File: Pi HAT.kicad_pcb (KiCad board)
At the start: 4 copper layers, 65 x 41.5 mm, 72 parts, among them IC1 AD7730, J1 Screw_Terminal_01x04, J11 Conn_01x02_Male, J4 Barrel_Jack, J5 Screw_Terminal_01x03, J6 Screw_Terminal_01x03, J7 GPIO_CONNECTOR, J9 Conn_01x03_Male, K1 SANYOU_SRD_Form_C, K2 SANYOU_SRD_Form_C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

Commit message: Updated wiring. Test points only added for AD7730.
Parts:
- removed TP1, TP2, TP3, TP4: TestPoint, TestPoint:TestPoint_Pad_D1.5mm
- moved R5 8.51 mm to (127.5, 106.7)
- moved R3 0.20 mm to (148.2, 123.0)
- moved C1 0.15 mm to (174.3, 108.6)
- moved C2 0.15 mm to (174.3, 105.6)
- moved R15 0.11 mm to (129.7, 117.6)
- moved C9 0.10 mm to (129.8, 118.6)
- moved JP2 0.08 mm to (137.1, 108.8)
- moved C12 0.06 mm to (125.2, 128.1)
- moved JP3 0.06 mm to (151.3, 108.8)
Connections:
- U1 pad 1: /GPIO16_SPI_CE2_N -> /GPIO8_SPI_CE0_N
- U1 pad 10: /GPIO16_SPI_CE2_N -> /GPIO8_SPI_CE0_N
- U1 pad 11: /GPIO19_SPI_MISO -> /GPIO9_SPI_MISO
- U1 pad 13: /GPIO16_SPI_CE2_N -> /GPIO8_SPI_CE0_N
- U1 pad 2: /GPIO21_SPI_SCLK -> /GPIO11_SPI_SCLK
- U1 pad 4: /GPIO16_SPI_CE2_N -> /GPIO8_SPI_CE0_N
- U1 pad 5: /GPIO20_SPI_MOSI -> /GPIO10_SPI_MOSI
- U1 pad 9: /GPIO16_SPI_CE2_N -> /GPIO8_SPI_CE0_N
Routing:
- net /GPIO8_SPI_CE0_N: track 0.00 -> 93.6 mm, vias 0 -> 5
- net +3V3: track 9.73 -> 82.4 mm, vias 0 -> 5
- net /GPIO9_SPI_MISO: track 31.5 -> 81.8 mm, vias 1 -> 3
- net /GPIO11_SPI_SCLK: track 34.3 -> 77.9 mm, vias 1 -> 2
- net /GPIO10_SPI_MOSI: track 30.3 -> 71.6 mm, vias 1 -> 3
- net /GPIO22_GEN3: track 0.00 -> 29.3 mm
- net GND: track 11.0 -> 36.3 mm, vias 0 -> 11
- net /GPIO16_SPI_CE2_N: track 22.1 -> 0.00 mm, vias 3 -> 0
- net /GPIO26: track 28.2 -> 11.4 mm
- net +5V: track 55.9 -> 70.6 mm
- net /GPIO20_SPI_MOSI: track 13.2 -> 0.00 mm
- net /Power Monitor/ADC0: track 0.00 -> 13.2 mm, vias 0 -> 1
- net Net-(JP6-Pad1): track 0.00 -> 11.9 mm, vias 0 -> 2
- net /Relays/COM2: track 17.7 -> 29.2 mm, vias 0 -> 3
- net /GPIO21_SPI_SCLK: track 11.1 -> 0.00 mm, vias 1 -> 0
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- removed copper zone on F.Cu, net GND
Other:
- copper layers 4 -> 2
- board text added: "Jumper"

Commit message: Updated wiring.
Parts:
- added G***: LOGO, LOGO, F.Cu at (172.4, 124.0)
- moved R9 2.69 mm to (119.4, 112.5), turned to 180 degrees
- moved D3 1.99 mm to (119.8, 110.3), turned to 90 degrees
- moved R16 0.19 mm to (158.1, 121.9)
- moved D1 0.19 mm to (156.5, 120.2)
- moved D4 0.19 mm to (155.6, 122.2)
- moved D5 0.17 mm to (138.7, 122.3)
- moved J9 0.14 mm to (125.0, 130.5)
- moved D2 0.09 mm to (139.5, 120.3)
- moved R17 0.09 mm to (141.2, 122.0)
- moved C1 0.06 mm to (174.3, 108.6)
- moved C2 0.06 mm to (174.3, 105.6)
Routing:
- net +5V: track 70.6 -> 197.1 mm, vias 2 -> 14
- net /GPIO5: track 0.00 -> 54.4 mm, vias 0 -> 2
- net GND: track 36.3 -> 75.7 mm, vias 11 -> 15
- net /GPIO26: track 11.4 -> 33.4 mm, vias 2 -> 4
- net /Relays/DC_SIDE2: track 16.4 -> 25.5 mm
- net /GPIO8_SPI_CE0_N: track 93.6 -> 96.5 mm
- net /Power Monitor/ADC0: track 13.2 -> 11.2 mm
- net /GPIO10_SPI_MOSI: track 71.6 -> 72.6 mm
- net /GPIO11_SPI_SCLK: track 77.9 -> 78.8 mm
- net /GPIO9_SPI_MISO: track 81.8 -> 82.7 mm
- net /Power Monitor/ADC6: track 15.4 -> 14.6 mm
- net /Power Monitor/ADC7: track 12.6 -> 13.3 mm
- net /Relays/DC_SIDE1: track 24.6 -> 24.9 mm, vias 0 -> 1
- added copper zone on F.Cu, net +5V
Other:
- board text added: "Pi Zero HAT Montso Mokake XX/12/2022"

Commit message: Updated via sizes on wiring.
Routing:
- net GND: track 75.7 -> 77.3 mm, vias 15 -> 17
- net +3V3: track 82.4 -> 83.2 mm, vias 5 -> 6
- net +5V: track 197.1 -> 197.7 mm, vias 14 -> 16

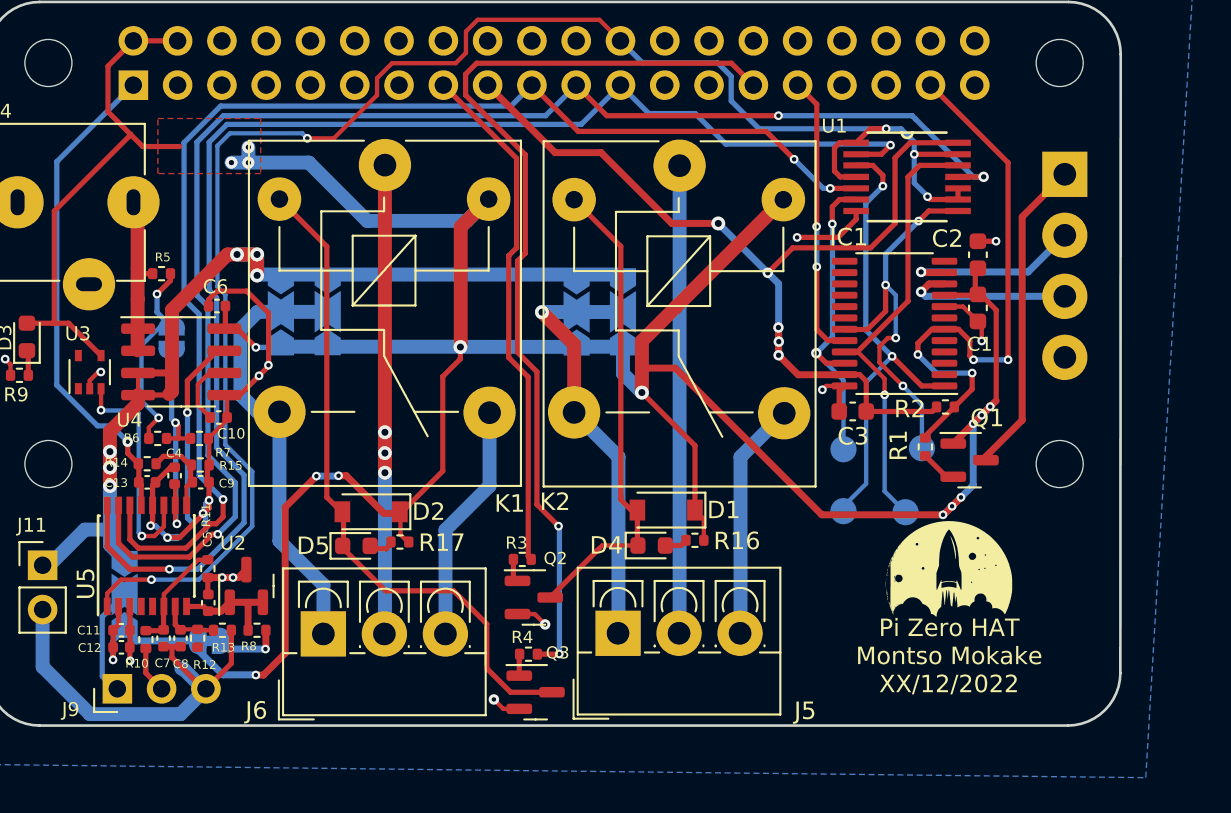
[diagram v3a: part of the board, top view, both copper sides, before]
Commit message: Used Phoenix connectors. Wired ADC0 track.
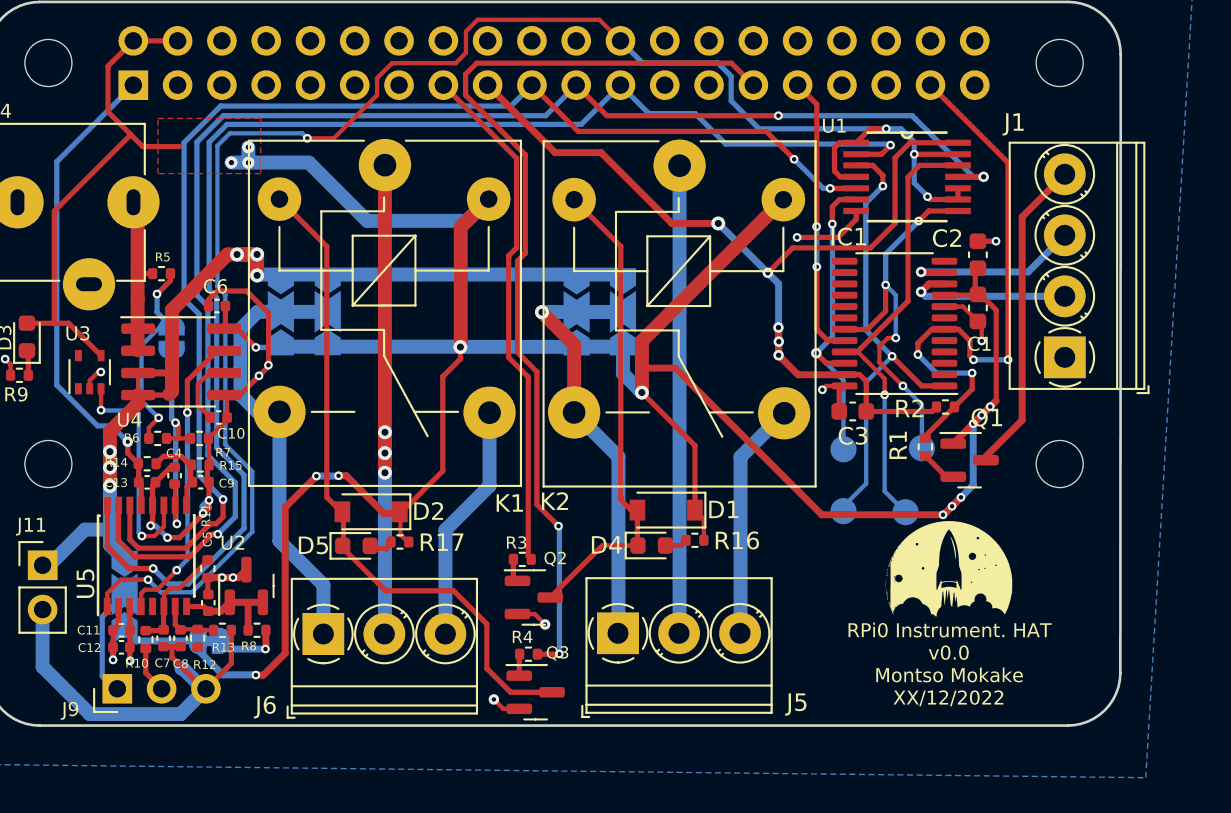
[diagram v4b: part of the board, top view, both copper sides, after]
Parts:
- J1: footprint TerminalBlock_4Ucon:TerminalBlock_4Ucon_1x04_P3.50mm_Vertical -> TerminalBlock_Phoenix:TerminalBlock_Phoenix_PT-1,5-4-3.5-H_1x04_P3.50mm_Horizontal; moved to F.Cu
- J5, J6: footprint TerminalBlock_4Ucon:TerminalBlock_4Ucon_1x03_P3.50mm_Vertical -> TerminalBlock_Phoenix:TerminalBlock_Phoenix_PT-1,5-3-3.5-H_1x03_P3.50mm_Horizontal
- moved J1 10.5 mm to (179.3, 111.5), turned to 90 degrees
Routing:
- net /Power Monitor/ADC0: track 11.2 -> 17.3 mm, vias 1 -> 2
- net GND: track 77.3 -> 75.8 mm
- net /GPIO11_SPI_SCLK: track 78.6 -> 79.4 mm
- net /GPIO8_SPI_CE0_N: track 96.1 -> 96.9 mm
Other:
- board text added: "RPi0 Instrument. HAT v0.0 Montso Mokake XX/12/2022"
- board text removed: "Pi Zero HAT Montso Mokake XX/12/2022"

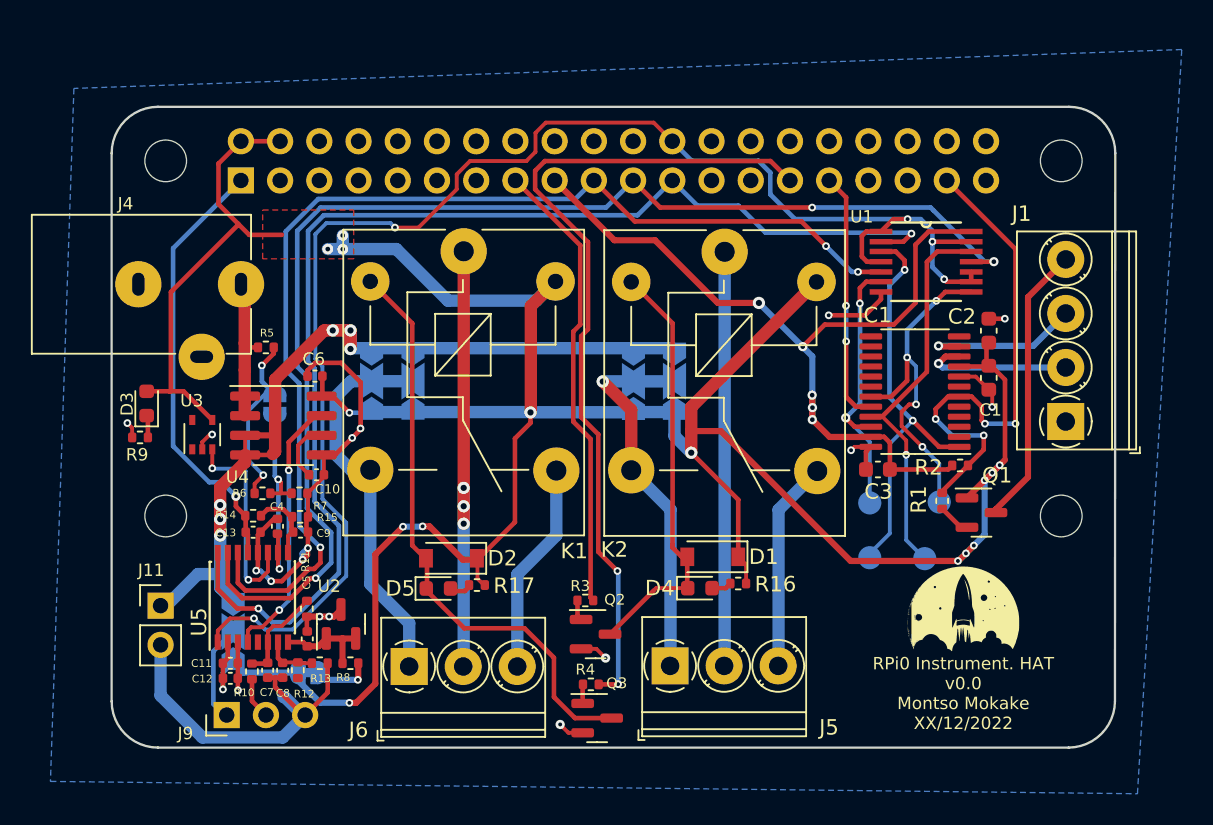
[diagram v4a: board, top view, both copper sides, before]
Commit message: Fixed CE pins. Added GND copper pour on F.Cu.
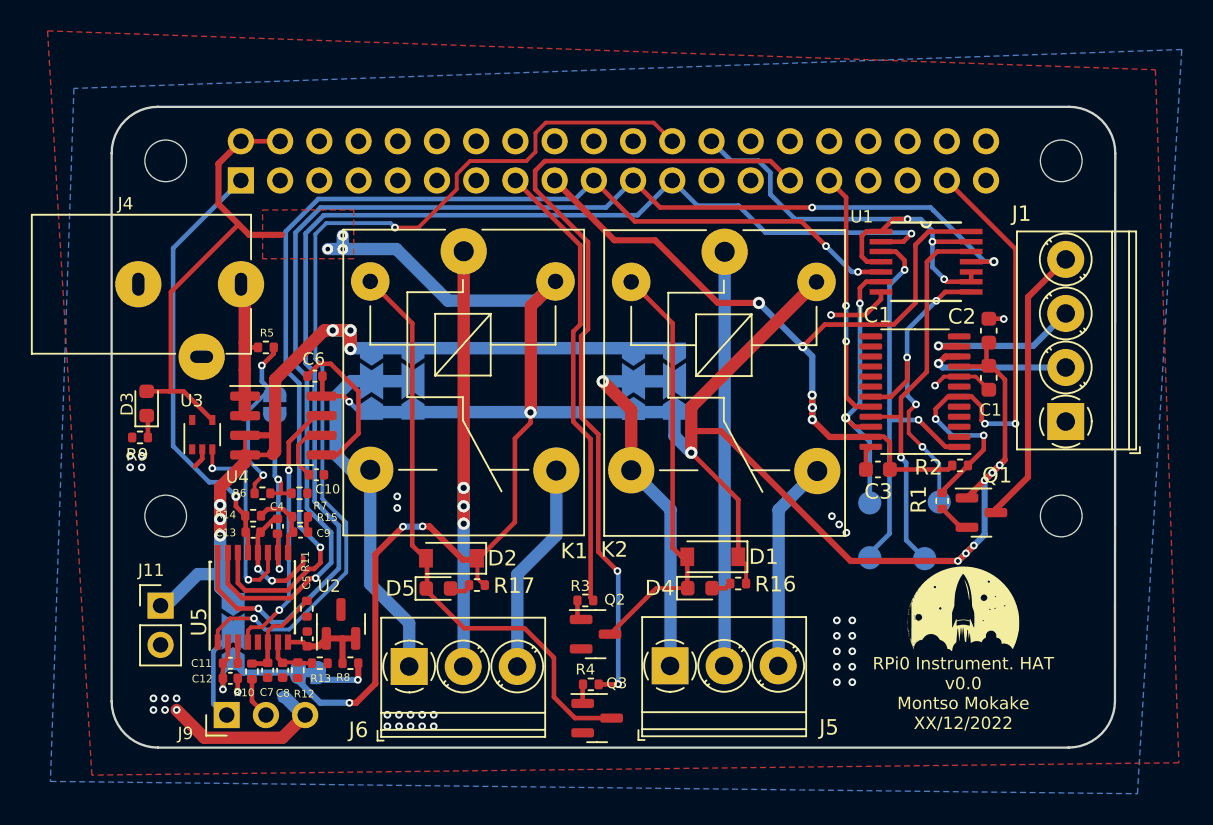
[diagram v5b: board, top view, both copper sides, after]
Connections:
- U1 pad 1: /GPIO8_SPI_CE0_N -> /GPIO7_SPI_CE1_N
- U1 pad 10: /GPIO8_SPI_CE0_N -> /GPIO7_SPI_CE1_N
- U1 pad 13: /GPIO8_SPI_CE0_N -> /GPIO7_SPI_CE1_N
- U1 pad 4: /GPIO8_SPI_CE0_N -> /GPIO7_SPI_CE1_N
- U1 pad 9: /GPIO8_SPI_CE0_N -> /GPIO7_SPI_CE1_N
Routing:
- net /GPIO8_SPI_CE0_N: track 96.9 -> 62.1 mm, vias 5 -> 2
- net /GPIO7_SPI_CE1_N: track 0.00 -> 32.1 mm, vias 0 -> 3
- net GND: track 75.8 -> 45.3 mm, vias 17 -> 41
- net /Instumentaional Amp/SPI_!CS_BUFF: track 22.5 -> 21.9 mm
- net /Instumentaional Amp/SPI_MISO_BUFF: track 26.2 -> 25.6 mm
- added copper zone on F.Cu, net GND

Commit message: Review and fixes on schematic and pcb.
-Updated Relay LED values.
-Fixed !RDY and R1 pin conflict on GPIO26.
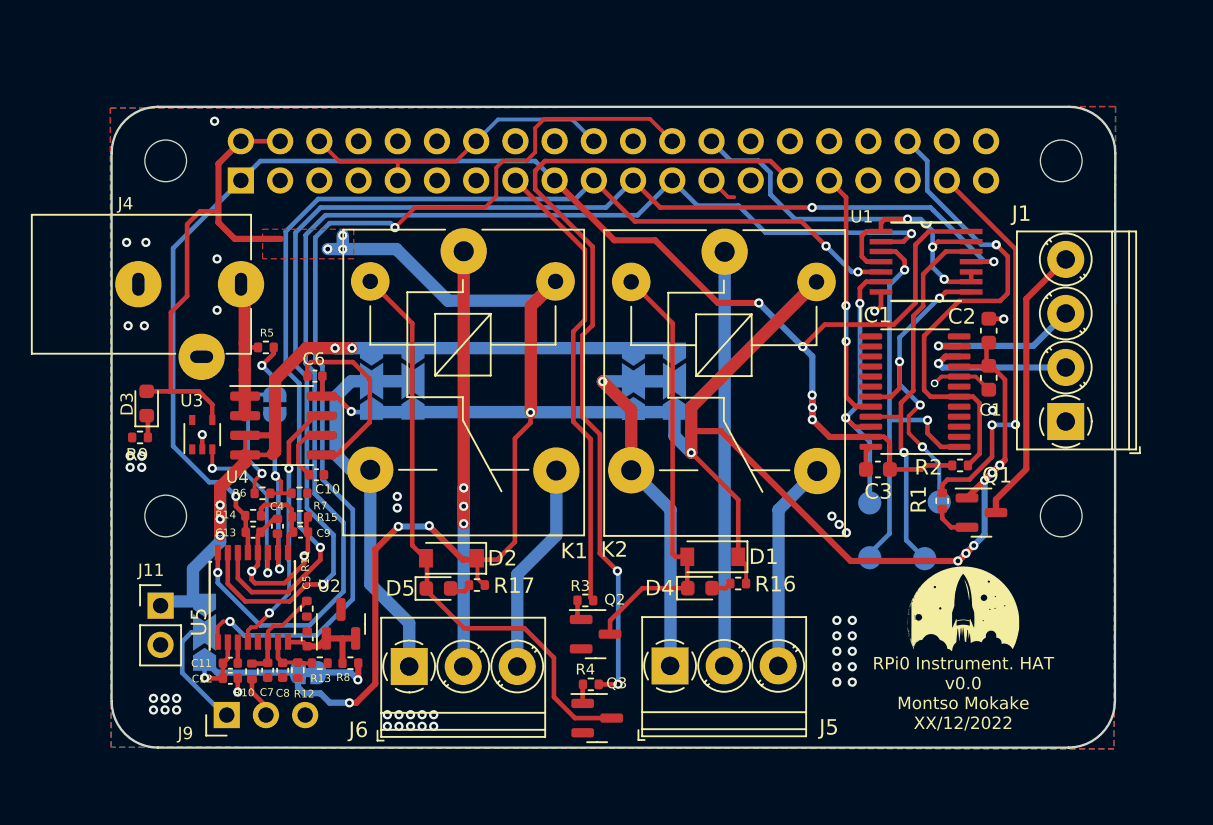
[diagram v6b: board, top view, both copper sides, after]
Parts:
- D4, D5: value LED_Small -> Blue_LED
- R16, R17: value 1k -> 120R
- moved JP7 1.85 mm to (123.5, 125.1)
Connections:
- IC1 pad 6: /GPIO26 -> /GPIO16
- J7 pad 36: /GPIO16_SPI_CE2_N -> /GPIO16
- R2 pad 1: /GPIO26 -> /GPIO16
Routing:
- net /GPIO16: track 0.00 -> 31.5 mm, vias 0 -> 1
- net +3V3: track 83.2 -> 104.6 mm
- net GND: track 45.3 -> 58.8 mm, vias 41 -> 50
- net /GPIO26: track 33.4 -> 25.8 mm, vias 4 -> 2
- net +5V: track 197.7 -> 202.5 mm
- net /Power Monitor/Batt_Sensed: track 58.0 -> 53.4 mm, vias 6 -> 5
- net /GPIO8_SPI_CE0_N: track 62.1 -> 64.8 mm
- net /Power Monitor/ADC7: track 13.3 -> 11.9 mm
- net Net-(J9-Pad1): track 6.43 -> 7.79 mm
- net /GPIO11_SPI_SCLK: track 79.4 -> 80.6 mm
- net /Power Monitor/ADC5: track 4.74 -> 5.55 mm
- net /GPIO9_SPI_MISO: track 82.7 -> 83.5 mm
- net Net-(D1-Pad2): track 27.8 -> 28.5 mm

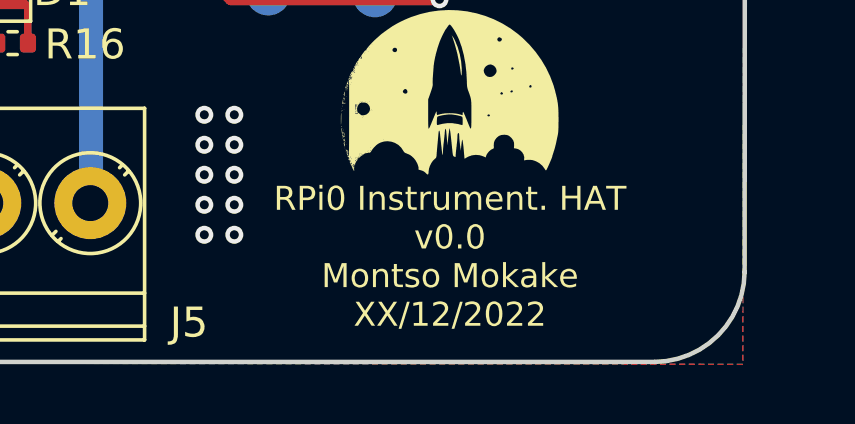
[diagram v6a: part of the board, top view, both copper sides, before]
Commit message: Update Pi HAT.kicad_pcb
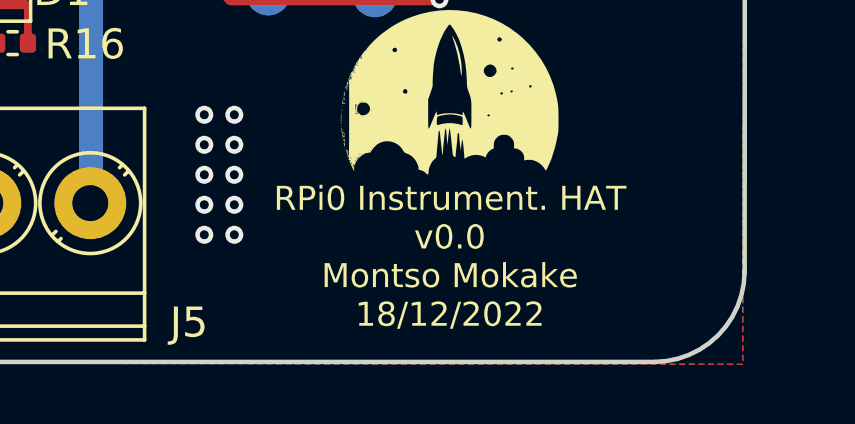
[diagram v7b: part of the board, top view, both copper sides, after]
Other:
- board text added: "RPi0 Instrument. HAT v0.0 Montso Mokake 18/12/2022"
- board text removed: "RPi0 Instrument. HAT v0.0 Montso Mokake XX/12/2022"
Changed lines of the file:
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@@
   (gr_line (start 182.532 94.068) (end 182.51068 129.568) (layer "Edge.Cuts") (width 0.15))
   (gr_line (start 179.532 91.068) (end 120.532 91.068) (layer "Edge.Cuts") (width 0.15))
-  (gr_text "RPi0 Instrument. HAT\nv0.0\nMontso Mokake\nXX/12/2022" (at 172.69 129.06) (layer "F.SilkS")
+  (gr_text "RPi0 Instrument. HAT\nv0.0\nMontso Mokake\n18/12/2022" (at 172.69 129.06) (layer "F.SilkS")
     (effects (font (size 0.8 0.8) (thickness 0.13)))
   )
